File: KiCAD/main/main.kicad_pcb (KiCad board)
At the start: 2 copper layers, 76 x 80 mm, 31 parts, among them IC1 DHT22, J1 Sound Sensor, J2 BuckConverter, J3 Charge Controller, J4 Battery Status, J5 Anemometer, J6 Conn_02x04_Odd_Even, SW1 SW_SPDT, SW2 BOOT, SW3 RESET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

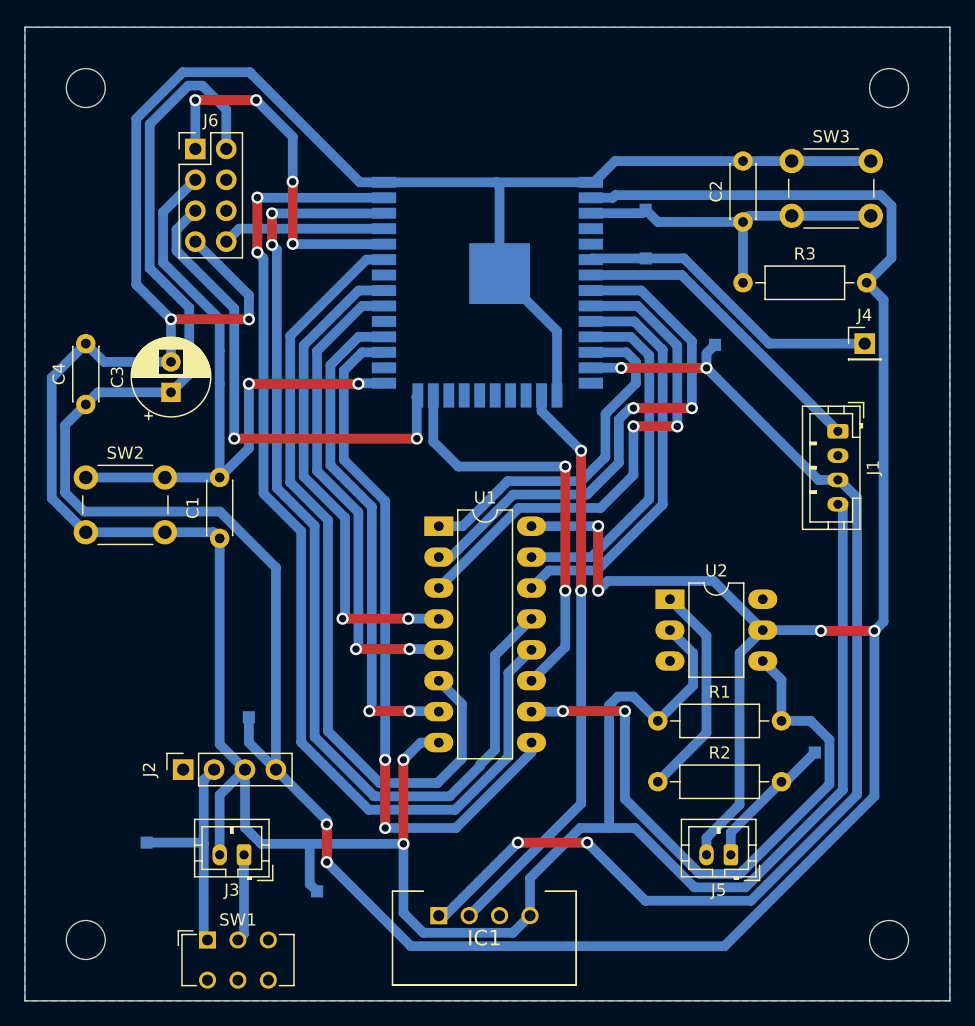
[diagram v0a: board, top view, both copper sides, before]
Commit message: increase via pad to 1.1mm and allow space for fixtures
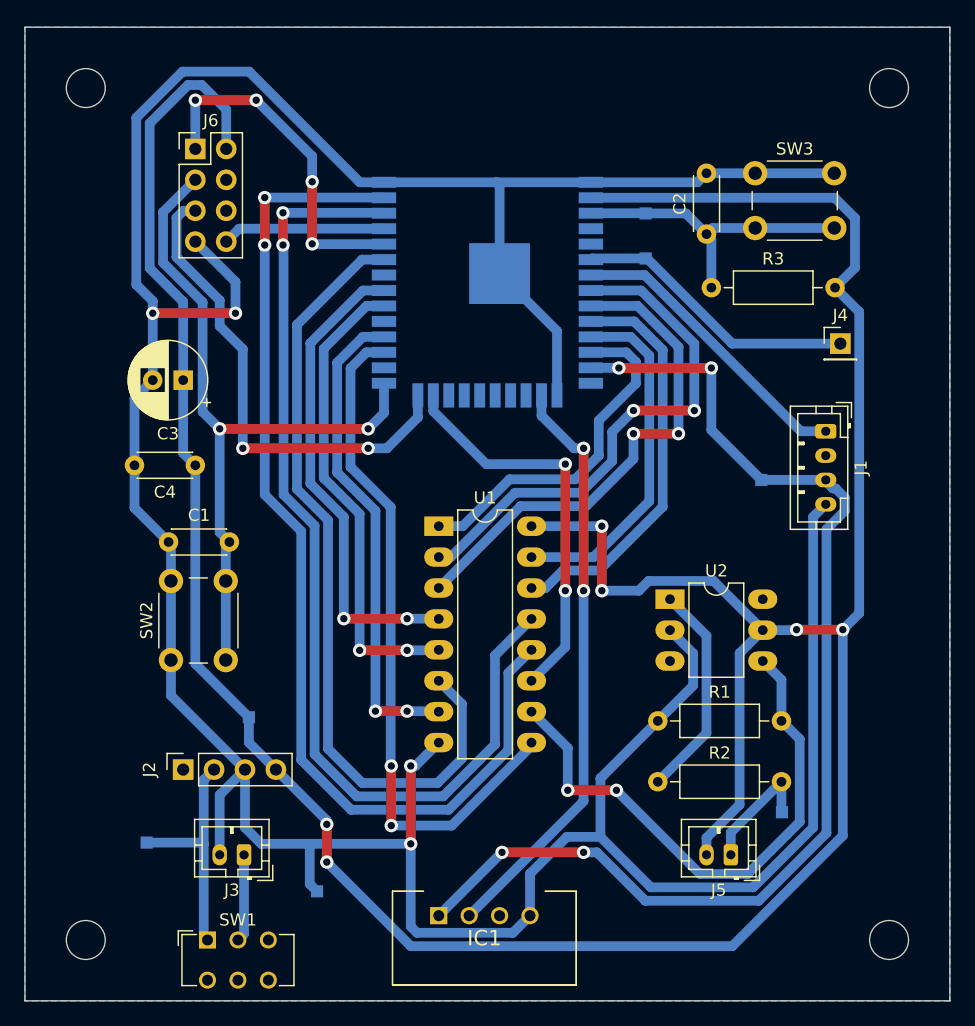
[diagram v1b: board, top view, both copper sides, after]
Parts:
- moved SW2 16.6 mm to (122.0, 102.0), turned to 90 degrees
- moved TP5 11.7 mm to (170.5, 87.2)
- moved C4 10.3 mm to (124.0, 86.0), turned to 180 degrees
- moved TP6 5.59 mm to (172.2, 114.5)
- moved C1 4.21 mm to (121.8, 92.3), turned to 0 degrees
- moved C2 3.16 mm to (166.0, 67.0)
- moved SW3 3.16 mm to (170.0, 62.0)
- moved R3 2.63 mm to (166.4, 71.4)
- moved J4 2.00 mm to (177.0, 76.0)
- moved C3 1.41 mm to (123.0, 79.0), turned to 180 degrees
- moved J1 1.00 mm to (175.8, 83.2)
- moved TP7 0.30 mm to (161.0, 65.3)
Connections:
- SW2 pad 1: /Microcontroller/IO0 -> GND
- SW2 pad 2: GND -> /Microcontroller/IO0
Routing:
- net +3V3: track 286.3 -> 255.9 mm
- net GND: track 320.8 -> 293.0 mm
- net /Opto_Anemometer_Out: track 51.1 -> 45.9 mm
- net /Microcontroller/EN: track 28.7 -> 25.5 mm
- net /Battery_status: track 25.4 -> 23.4 mm
- net /Microcontroller/IO16: track 58.3 -> 56.8 mm
- net /reset_counter: track 34.2 -> 32.9 mm
- net /Anemometer_Out: track 11.5 -> 10.2 mm
- net /Microcontroller/IO0: track 58.3 -> 59.4 mm
- net /Microcontroller/IO17: track 41.0 -> 39.9 mm
- net /Sound_Signal: track 25.6 -> 24.6 mm
- net /Microcontroller/RXD0: track 29.6 -> 28.6 mm
- net /Microcontroller/IO18: track 39.8 -> 38.9 mm
- net /Microcontroller/IO19: track 40.3 -> 39.4 mm
- net /supply_on: track 95.3 -> 94.5 mm
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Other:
- net class Default: via_dia 0.8 -> 1.1; via_drill 0.4 -> 0.6
- rule via_min_drill: 0.3 -> 0.6
- rule via_min_size: 0.8 -> 1.1

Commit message: Replace DHT22 and cound sensor JST connector with GROVE connectors
Also replace mounting holes and add them to the reference schematic
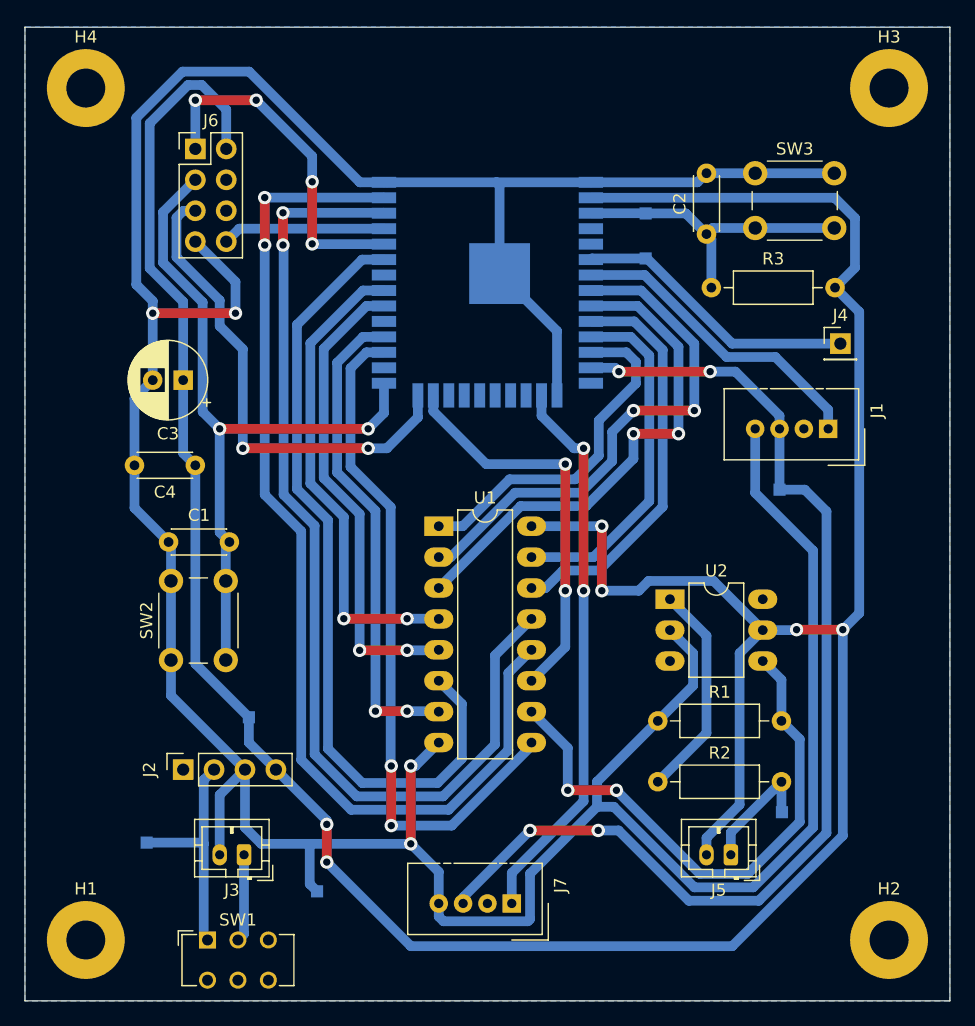
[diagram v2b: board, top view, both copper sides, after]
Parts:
- removed IC1: DHT22, Local:DHT22
- removed REF** (x4): MountingHole_3.2mm_M3, MountingHole:MountingHole_3.2mm_M3
- added H1: MountingHole, MountingHole:MountingHole_3.2mm_M3_Pad, F.Cu at (115.0, 125.0)
- added H2: MountingHole, MountingHole:MountingHole_3.2mm_M3_Pad, F.Cu at (181.0, 125.0)
- added H3: MountingHole, MountingHole:MountingHole_3.2mm_M3_Pad, F.Cu at (181.0, 55.0)
- added H4: MountingHole, MountingHole:MountingHole_3.2mm_M3_Pad, F.Cu at (115.0, 55.0)
- added J7: DHT22, Connector:NS-Tech_Grove_1x04_P2mm_Vertical, F.Cu at (150.0, 122.0)
- J1: footprint Connector_JST:JST_PH_B4B-PH-K_1x04_P2.00mm_Vertical -> Connector:NS-Tech_Grove_1x04_P2mm_Vertical
- moved TP5 1.70 mm to (172.0, 88.0)
- moved J1 0.28 mm to (176.0, 83.0)
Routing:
- net GND: track 293.0 -> 297.9 mm
- net /supply_on: track 94.5 -> 91.6 mm
- net /DHT22_Data: track 48.5 -> 46.1 mm
- net /Sound_Signal: track 24.6 -> 25.6 mm

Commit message: Increase margins for the fixtures
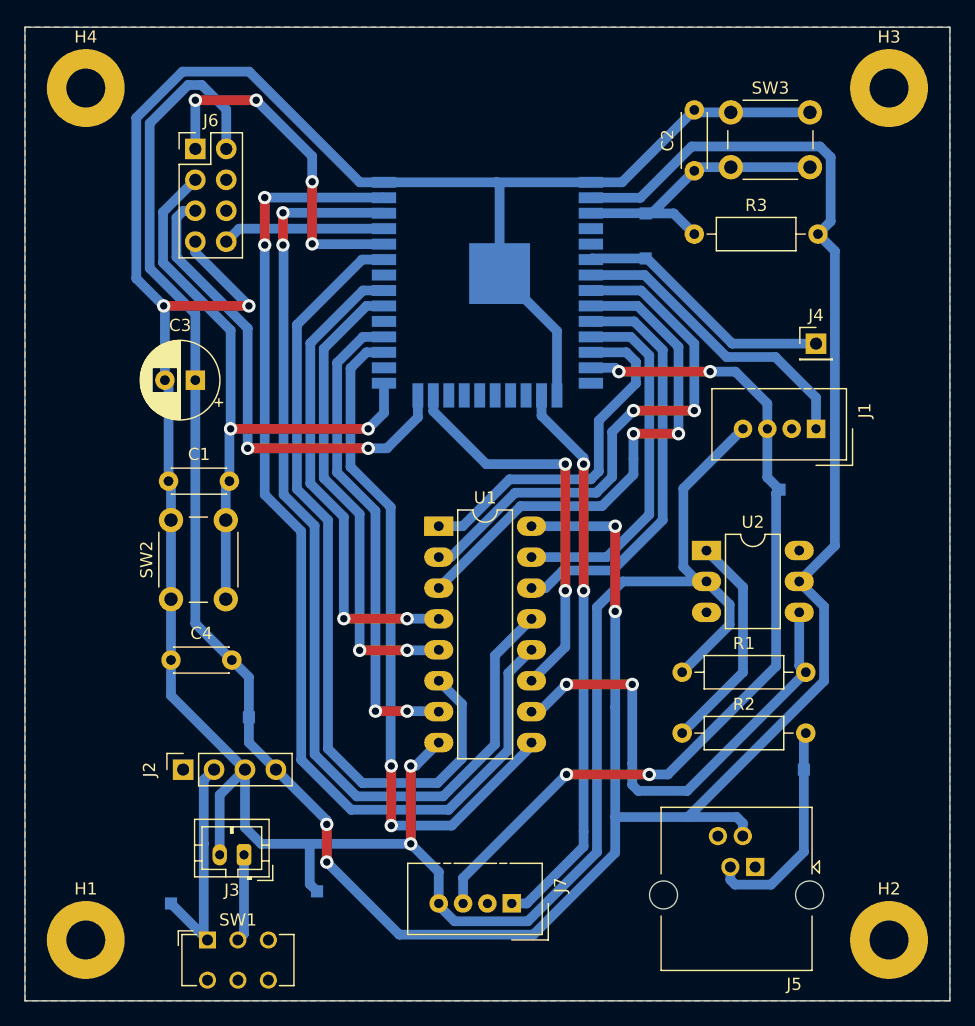
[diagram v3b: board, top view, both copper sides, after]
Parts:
- J5: footprint Connector_JST:JST_PH_B2B-PH-K_1x02_P2.00mm_Vertical -> Connector_RJ:RJ14_Connfly_DS1133-S4_Horizontal
- moved C4 16.1 mm to (122.0, 102.0), turned to 0 degrees
- moved SW3 5.39 mm to (168.0, 57.0)
- moved TP2 5.39 mm to (122.0, 122.0)
- moved C2 5.30 mm to (165.0, 61.8)
- moved C1 5.00 mm to (121.8, 87.3)
- moved SW2 5.00 mm to (122.0, 97.0)
- moved U2 5.00 mm to (166.0, 93.0)
- moved R3 4.62 mm to (165.0, 67.0)
- moved R1 4.47 mm to (164.0, 103.0)
- moved R2 4.47 mm to (164.0, 108.0)
- moved TP6 3.94 mm to (174.0, 111.0)
- moved J5 2.24 mm to (170.0, 119.0)
- moved J4 2.00 mm to (175.0, 76.0)
- moved C3 1.00 mm to (124.0, 79.0)
- moved J1 1.00 mm to (175.0, 83.0)
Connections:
- C4 pad 1: +3V3 -> GND
- C4 pad 2: GND -> +3V3
- J5 pad 1: /Anemometer_Out -> Net-(J5-Pad1)
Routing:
- net GND: track 297.9 -> 272.5 mm
- net +3V3: track 255.9 -> 236.5 mm, vias 6 -> 4
- net /supply_on: track 91.6 -> 72.9 mm
- net /Anemometer_Out: track 10.2 -> 18.2 mm
- net /Microcontroller/IO0: track 59.4 -> 53.6 mm
- net /Opto_Anemometer_Out: track 45.9 -> 41.1 mm
- net /Battery_status: track 23.4 -> 21.4 mm
- net /Microcontroller/EN: track 25.5 -> 24.3 mm
- net /Microcontroller/IO33: track 41.9 -> 42.7 mm
- net /Microcontroller/IO27: track 28.5 -> 29.3 mm
- net /Microcontroller/IO32: track 43.2 -> 44.0 mm
- net /Microcontroller/IO26: track 29.0 -> 29.6 mm
- net /Microcontroller/IO25: track 33.3 -> 34.0 mm
- added copper zone on F.Cu, net (none)

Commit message: Re-annotate connectors
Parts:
- renumbered J3 to J1, J4 to J3, J6 to J4, J1 to J5, J7 to J6, J5 to J7

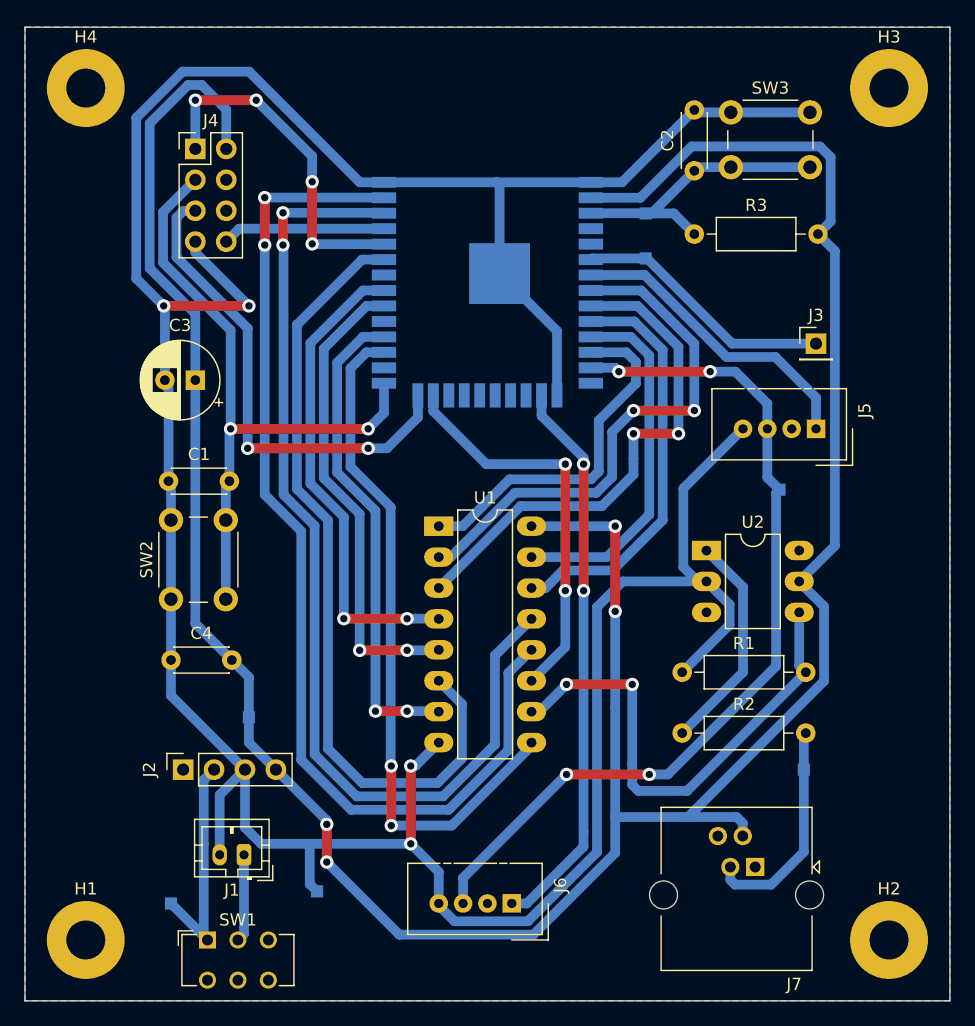
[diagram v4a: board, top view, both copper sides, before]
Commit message: Improve placement of the Power switch, RJ14, J3 and J5 connectors
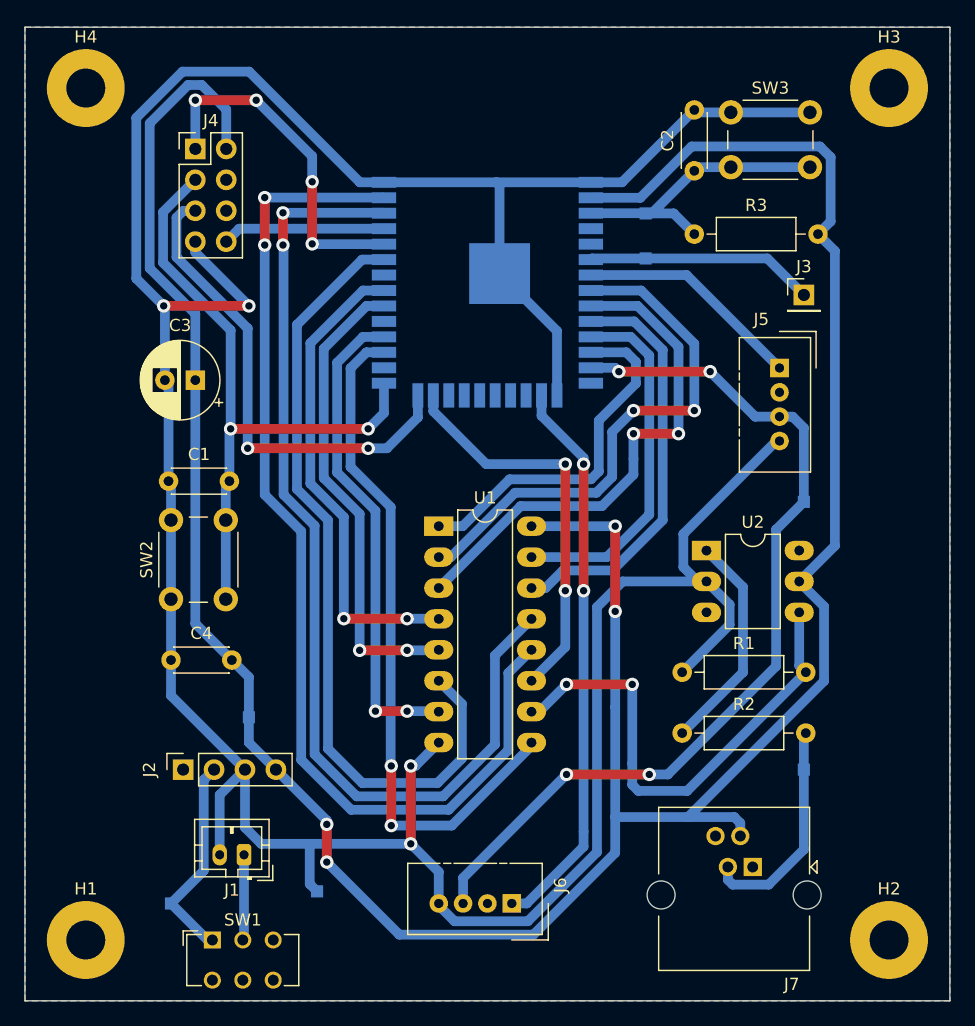
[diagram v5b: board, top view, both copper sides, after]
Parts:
- moved J5 5.83 mm to (172.0, 78.0), turned to 0 degrees
- moved J3 4.12 mm to (174.0, 72.0)
- moved TP5 2.24 mm to (174.0, 89.0)
- moved SW1 0.40 mm to (125.4, 125.0)
- moved J7 0.20 mm to (169.8, 119.0)
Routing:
- net /Sound_Signal: track 25.2 -> 18.7 mm
- net /Battery_status: track 21.4 -> 18.8 mm
- net /supply_on: track 72.9 -> 75.1 mm
- net /Vin_Buck: track 18.7 -> 17.1 mm
